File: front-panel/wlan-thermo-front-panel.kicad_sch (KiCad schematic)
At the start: 28 parts, among them IC1 ME6211C33M5G-N, J2 Conn_01x02, J3 Conn_01x02, J3 PROG_HDR, Q1 SS8050-G, Q2 SS8050-G, SW1 SW_Push, SW4 RotaryEncoder_Switch, U1 ESP-12F, U2 SHT4x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

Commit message: Fixed strapping pins for booting and loading
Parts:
- added R11, R12, R13: 10k, Resistor_SMD:R_0603_1608Metric_Pad0.98x0.95mm_HandSolder, symbol Device:R
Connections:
- net +3V3: now also R11.1, R13.1
- net GND: now also R12.2
- net ~{GPIO0}: now also R13.2
- net at U1.17 (GPIO2): now also R11.2
- net GPIO16_RELAY: now reaches U1.4 (GPIO16)
- net GPIO16_RELAY: now also J3.1 (Pin_1)
- net GPIO15_RELAY: no longer names the net of U1.16 (GPIO15)
- net GPIO15_RELAY: now also R12.1; no longer J3.1 (Pin_1)
- no-connect marks 11 -> 9

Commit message: Changed strapping pins to resistor network
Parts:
- removed R10, R11, R13, R9: 10k, Resistor_SMD:R_0603_1608Metric_Pad0.98x0.95mm_HandSolder, symbol Device:R
- added RN1: 10k, YC164JR07220RL, symbol Chof747 passive:YC164-FR-0710KL
- F1: footprint Fuse:Fuse_1206_3216Metric_Pad1.42x1.75mm_HandSolder -> Fuse:Fuse_0805_2012Metric_Pad1.15x1.40mm_HandSolder
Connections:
- net +3V3: now also RN1.5, RN1.6, RN1.7, RN1.8
- net GPIO4_SDA: now also RN1.4
- net GPIO5_SCL: now also RN1.3
- net ~{GPIO0}: now also RN1.1
- net GPIO2: now reaches U1.17 (GPIO2)
- net GPIO2: now also RN1.2

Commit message: Use UMH3N chip for autorestart cycle
- Removed Q1/Q2 and the two 10k resistors and replace it with UMH3N for autoreset
- Changed footprint of fuse to 0804
- Reorganised board to be smaller to fit into casing of existing wall switch
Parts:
- removed Q1, Q2: SS8050-G, Package_TO_SOT_SMD:SOT-23, symbol Device:Q_NPN_BCE
- removed R2, R3: 10k, Resistor_SMD:R_0603_1608Metric_Pad0.98x0.95mm_HandSolder, symbol Device:R
- added Q1: UMH3N, Package_TO_SOT_SMD:SOT-363_SC-70-6, symbol Transistor_BJT:UMH3N
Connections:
- net DTR: now also Q1.2 (B1), Q1.4 (E2)
- net RTS: now also Q1.1 (E1), Q1.5 (B2)
- net ~{GPIO0}: now also Q1.3 (C2)
- net ~{RESET}: now also Q1.6 (C1)
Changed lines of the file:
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@@
+    (stroke (width 0) (type default))
+  )
+  (wire (pts (xy 38.1 119.38) (xy 44.45 119.38))
     (stroke (width 0) (type default))
   )
@@
     (stroke (width 0) (type default))
   )
-  (wire (pts (xy 36.83 104.14) (xy 39.37 104.14))
+  (wire (pts (xy 36.83 104.14) (xy 44.45 104.14))
     (stroke (width 0) (type default))
   )
@@
   )
   (wire (pts (xy 67.31 66.04) (xy 69.85 66.04))
-    (stroke (width 0) (type default))
-  )
-  (wire (pts (xy 38.1 119.38) (xy 39.37 119.38))
     (stroke (width 0) (type default))
   )
@@
         (path "/e8426e51-e5a9-4642-8277-6d3f50e0e523"
           (reference "#PWR010") (unit 1)
-        )
-      )
-    )
-  )
-  (symbol (lib_id "Device:R") (at 43.18 119.38 90) (unit 1)
-    (in_bom yes) (on_board yes) (dnp no) (fields_autoplaced)
-    (property "Reference" "R3" (at 43.18 113.03 90)
-      (effects (font (size 1.27 1.27)))
-    )
-    (property "Value" "10k" (at 43.18 115.57 90)
-      (effects (font (size 1.27 1.27)))
-    )
-    (property "Footprint" "Resistor_SMD:R_0603_1608Metric_Pad0.98x0.95mm_HandSolder" (at 43.18 121.158 90)
-      (effects (font (size 1.27 1.27)) hide)
-    )
-    (property "Datasheet" "~" (at 43.18 119.38 0)
-      (effects (font (size 1.27 1.27)) hide)
-    )
-    (pin "1")
-    (pin "2")
-    (instances
-      (project "esp32-s3-dev-board"
-        (path "/9c0a2796-2802-493a-b118-8c7d4a430625"
-          (reference "R3") (unit 1)
-        )
-      )
-      (project "wlan-thermo-front-panel"
-        (path "/e8426e51-e5a9-4642-8277-6d3f50e0e523"
-          (reference "R2") (unit 1)
         )
       )
@@
     )
   )
+  (symbol (lib_id "Transistor_BJT:UMH3N") (at 49.53 104.14 0) (unit 1)
+    (in_bom yes) (on_board yes) (dnp no) (fields_autoplaced)
+    (property "Reference" "Q1" (at 57.15 103.505 0)
+      (effects (font (size 1.27 1.27)) (justify left))
+    )
+    (property "Value" "UMH3N" (at 57.15 106.045 0)
+      (effects (font (size 1.27 1.27)) (justify left))
+    )
+    (property "Footprint" "Package_TO_SOT_SMD:SOT-363_SC-70-6" (at 49.657 115.316 0)
+      (effects (font (size 1.27 1.27)) hide)
+    )
+    (property "Datasheet" "http://rohmfs.rohm.com/en/products/databook/datasheet/discrete/transistor/digital/emh3t2r-e.pdf" (at 53.34 104.14 0)
+      (effects (font (size 1.27 1.27)) hide)
+    )
+    (pin "1")
+    (pin "2")
+    (pin "6")
+    (pin "3")
+    (pin "4")
+    (pin "5")
+    (instances
+      (project "wlan-thermo-front-panel"
+        (path "/e8426e51-e5a9-4642-8277-6d3f50e0e523"
+          (reference "Q1") (unit 1)
+        )
+      )
+    )
+  )
   (symbol (lib_id "Device:R") (at 156.21 119.38 0) (unit 1)
     (in_bom yes) (on_board yes) (dnp no) (fields_autoplaced)
@@
     )
   )
-  (symbol (lib_id "Device:R") (at 43.18 104.14 90) (unit 1)
-    (in_bom yes) (on_board yes) (dnp no) (fields_autoplaced)
-    (property "Reference" "R2" (at 43.18 97.79 90)
-      (effects (font (size 1.27 1.27)))
-    )
-    (property "Value" "10k" (at 43.18 100.33 90)
-      (effects (font (size 1.27 1.27)))
-    )
-    (property "Footprint" "Resistor_SMD:R_0603_1608Metric_Pad0.98x0.95mm_HandSolder" (at 43.18 105.918 90)
-      (effects (font (size 1.27 1.27)) hide)
-    )
-    (property "Datasheet" "~" (at 43.18 104.14 0)
-      (effects (font (size 1.27 1.27)) hide)
-    )
-    (pin "1")
-    (pin "2")
-    (instances
-      (project "esp32-s3-dev-board"
-        (path "/9c0a2796-2802-493a-b118-8c7d4a430625"
-          (reference "R2") (unit 1)
-        )
-      )
-      (project "wlan-thermo-front-panel"
-        (path "/e8426e51-e5a9-4642-8277-6d3f50e0e523"
-          (reference "R1") (unit 1)
-        )
-      )
-    )
-  )
   (symbol (lib_id "Connector_Generic:Conn_01x02") (at 27.94 167.64 0) (unit 1)
     (in_bom yes) (on_board yes) (dnp no)
@@
     )
   )
-  (symbol (lib_id "Device:Q_NPN_BCE") (at 52.07 104.14 0) (unit 1)
-    (in_bom yes) (on_board yes) (dnp no) (fields_autoplaced)
-    (property "Reference" "Q1" (at 57.15 102.8699 0)
-      (effects (font (size 1.27 1.27)) (justify left))
-    )
-    (property "Value" "SS8050-G" (at 57.15 105.4099 0)
-      (effects (font (size 1.27 1.27)) (justify left))
-    )
-    (property "Footprint" "Package_TO_SOT_SMD:SOT-23" (at 57.15 101.6 0)
-      (effects (font (size 1.27 1.27)) hide)
-    )
-    (property "Datasheet" "~" (at 52.07 104.14 0)
-      (effects (font (size 1.27 1.27)) hide)
-    )
-    (pin "1")
-    (pin "2")
+  (symbol (lib_id "Transistor_BJT:UMH3N") (at 49.53 119.38 0) (mirror x) (unit 2)
+    (in_bom yes) (on_board yes) (dnp no)
+    (property "Reference" "Q1" (at 57.15 120.015 0)
+      (effects (font (size 1.27 1.27)) (justify left))
+    )
+    (property "Value" "UMH3N" (at 57.15 117.475 0)
+      (effects (font (size 1.27 1.27)) (justify left))
+    )
+    (property "Footprint" "Package_TO_SOT_SMD:SOT-363_SC-70-6" (at 49.657 108.204 0)
+      (effects (font (size 1.27 1.27)) hide)
+    )
+    (property "Datasheet" "http://rohmfs.rohm.com/en/products/databook/datasheet/discrete/transistor/digital/emh3t2r-e.pdf" (at 53.34 119.38 0)
+      (effects (font (size 1.27 1.27)) hide)
+    )
+    (pin "1")
+    (pin "2")
+    (pin "6")
     (pin "3")
-    (instances
-      (project "esp32-s3-dev-board"
-        (path "/9c0a2796-2802-493a-b118-8c7d4a430625"
-          (reference "Q1") (unit 1)
-        )
-      )
-      (project "wlan-thermo-front-panel"
-        (path "/e8426e51-e5a9-4642-8277-6d3f50e0e523"
-          (reference "Q1") (unit 1)
+    (pin "4")
+    (pin "5")
+    (instances
+      (project "wlan-thermo-front-panel"
+        (path "/e8426e51-e5a9-4642-8277-6d3f50e0e523"
+          (reference "Q1") (unit 2)
         )
       )
@@
         )
       )
-    )
-  )
-  (symbol (lib_id "Device:Q_NPN_BCE") (at 52.07 119.38 0) (mirror x) (unit 1)
-    (in_bom yes) (on_board yes) (dnp no) (fields_autoplaced)
-    (property "Reference" "Q2" (at 57.15 118.1099 0)
-      (effects (font (size 1.27 1.27)) (justify left))
-    )
-    (property "Value" "SS8050-G" (at 57.15 120.6499 0)
-      (effects (font (size 1.27 1.27)) (justify left))
-    )
-    (property "Footprint" "Package_TO_SOT_SMD:SOT-23" (at 57.15 121.92 0)
-      (effects (font (size 1.27 1.27)) hide)
-    )
-    (property "Datasheet" "~" (at 52.07 119.38 0)
-      (effects (font (size 1.27 1.27)) hide)
-    )
-    (pin "1")
-    (pin "2")
-    (pin "3")
-    (instances
-      (project "esp32-s3-dev-board"
-        (path "/9c0a2796-2802-493a-b118-8c7d4a430625"
-          (reference "Q2") (unit 1)
-        )
-      )
-      (project "wlan-thermo-front-panel"
-        (path "/e8426e51-e5a9-4642-8277-6d3f50e0e523"
-          (reference "Q2") (unit 1)
-        )
-      )

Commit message: Changed relay pin to avoid on on flash and boot
- Change relay pin to GPIO 13
- Change Rotary encoder pin to GPIO0 (also pulled up and provides extra feature: Rotary button works as flash button)
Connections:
- net GPIO13_RENBTN renamed GPIO13_RELAY
- net GPIO13_RELAY: now also J3.1 (Pin_1); no longer SW4.2 (NO)
- net GPIO16_RELAY: no longer names the net of U1.4 (GPIO16)
- net GPIO16_RELAY: no longer J3.1 (Pin_1)
- net ~{GPIO0} renamed ~{GPIO0_RENBTN_FLASH}
- net ~{GPIO0_RENBTN_FLASH}: now also SW4.2 (NO)
- no-connect marks 9 -> 10
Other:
- moved on the sheet: RN1

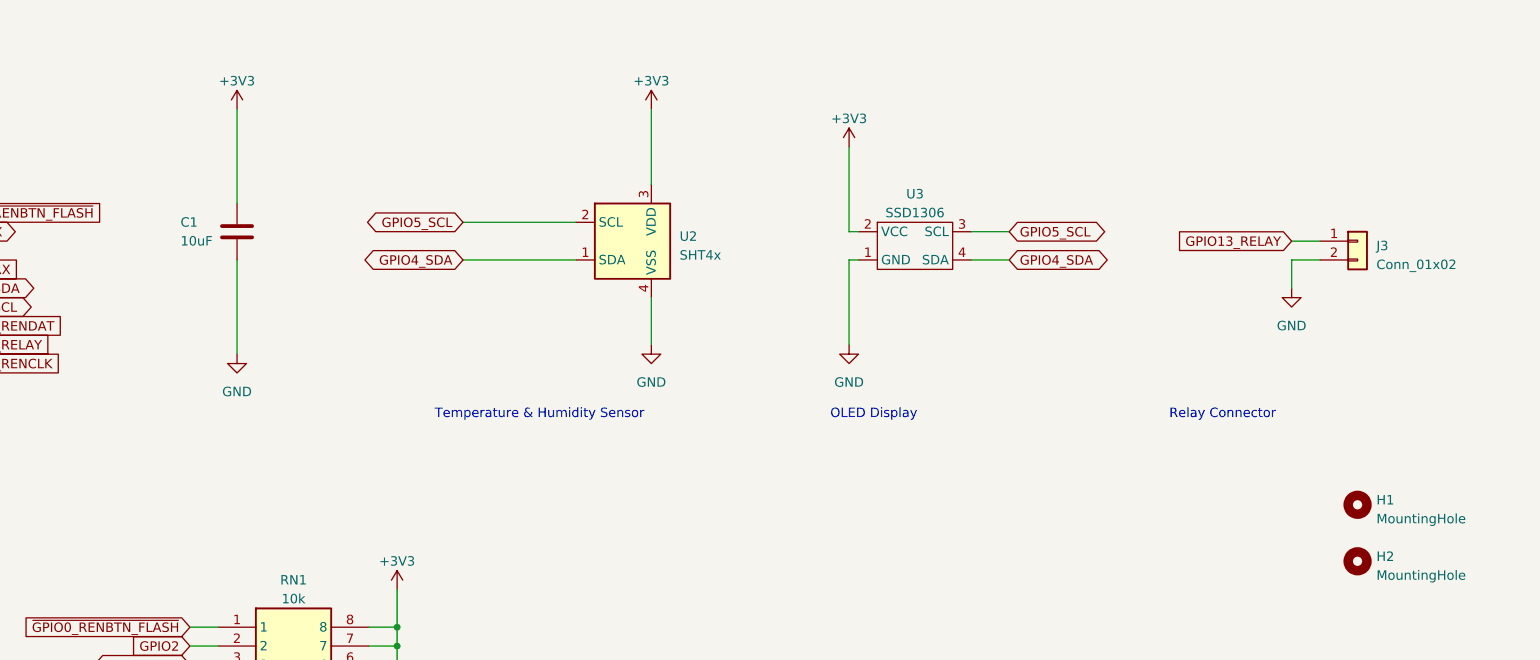
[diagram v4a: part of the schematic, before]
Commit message: external version of temp sensor
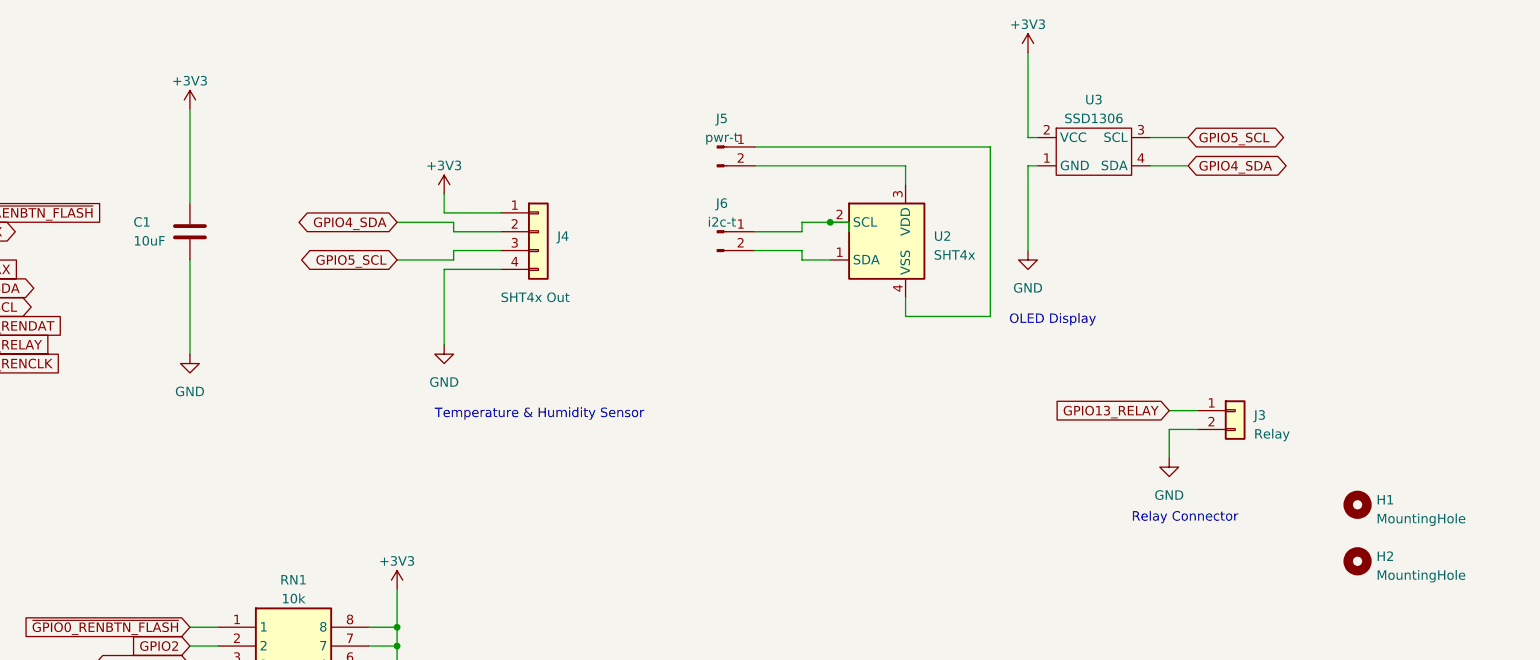
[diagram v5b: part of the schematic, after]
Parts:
- added J4: SHT4x Out, Chof747 Footprints:JUSHUO-AFC10-S04QCA 1x4 Horizontal (JST SH), symbol Connector_Generic:Conn_01x04
- added J5: pwr-t, Chof747 Footprints:Solder Pad 1x2 1.5x3, symbol Chof747 Connectors:Conn_01x02_Male
- added J6: i2c-t, Chof747 Footprints:Solder Pad 1x2 1.5x3, symbol Chof747 Connectors:Conn_01x02_Male
- J3: value Conn_01x02 -> Relay
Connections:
- net +3V3: now also J4.1 (Pin_1); no longer U2.3 (VDD)
- net GND: now also J4.4 (Pin_4); no longer U2.4 (VSS)
- net GPIO4_SDA: now also J4.2 (Pin_2); no longer U2.1 (SDA)
- net GPIO5_SCL: now also J4.3 (Pin_3); no longer U2.2 (SCL)
- new net: J5.1 (Pin_1), U2.4 (VSS)
- new net: J5.2 (Pin_2), U2.3 (VDD)
- new net: J6.2 (Pin_2), U2.1 (SDA)
- new net: J6.1 (Pin_1), U2.2 (SCL)
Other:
- moved on the sheet: C1, J3, U2, U3
